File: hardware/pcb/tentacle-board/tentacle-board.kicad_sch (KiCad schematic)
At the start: 32 parts, among them J1 USB_B_Micro, J2 Conn_01x02, U1 NCP1117-3.3_SOT223, U2 W25Q128JVS, U3 RP2040, Y1 ABLS-12.000MHZ-B4-T

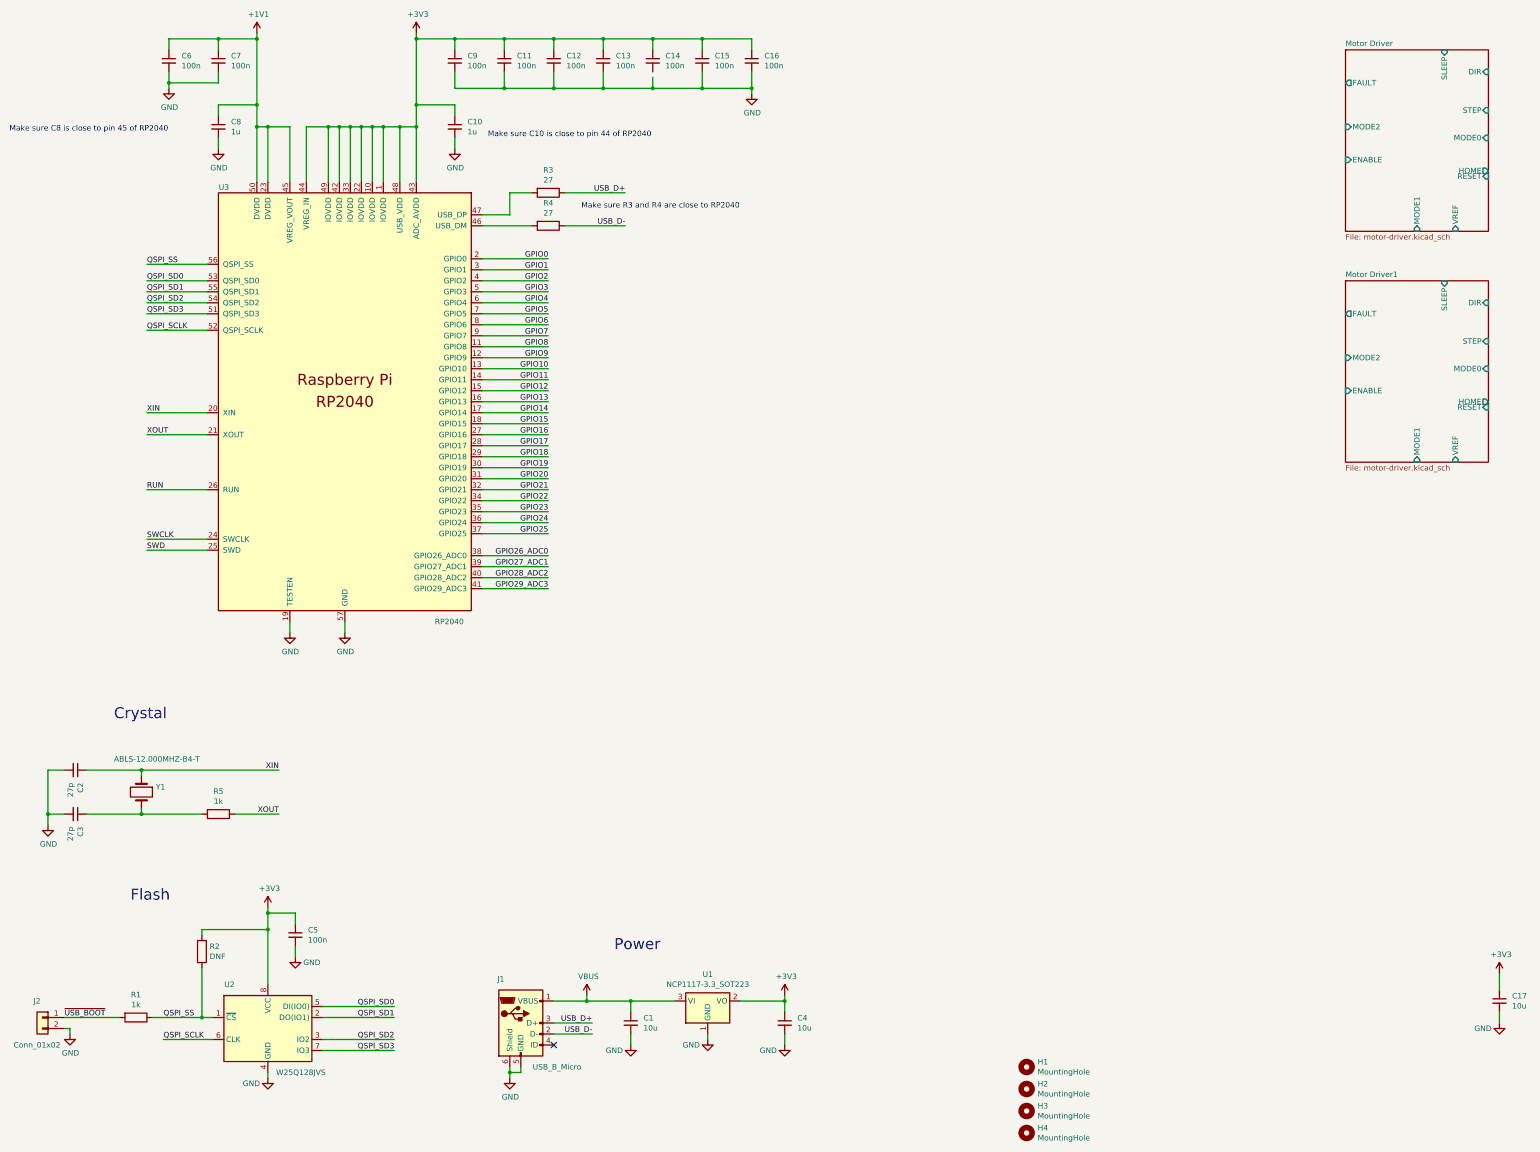
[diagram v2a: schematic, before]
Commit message: Added the MCU and supporting components and wired them up
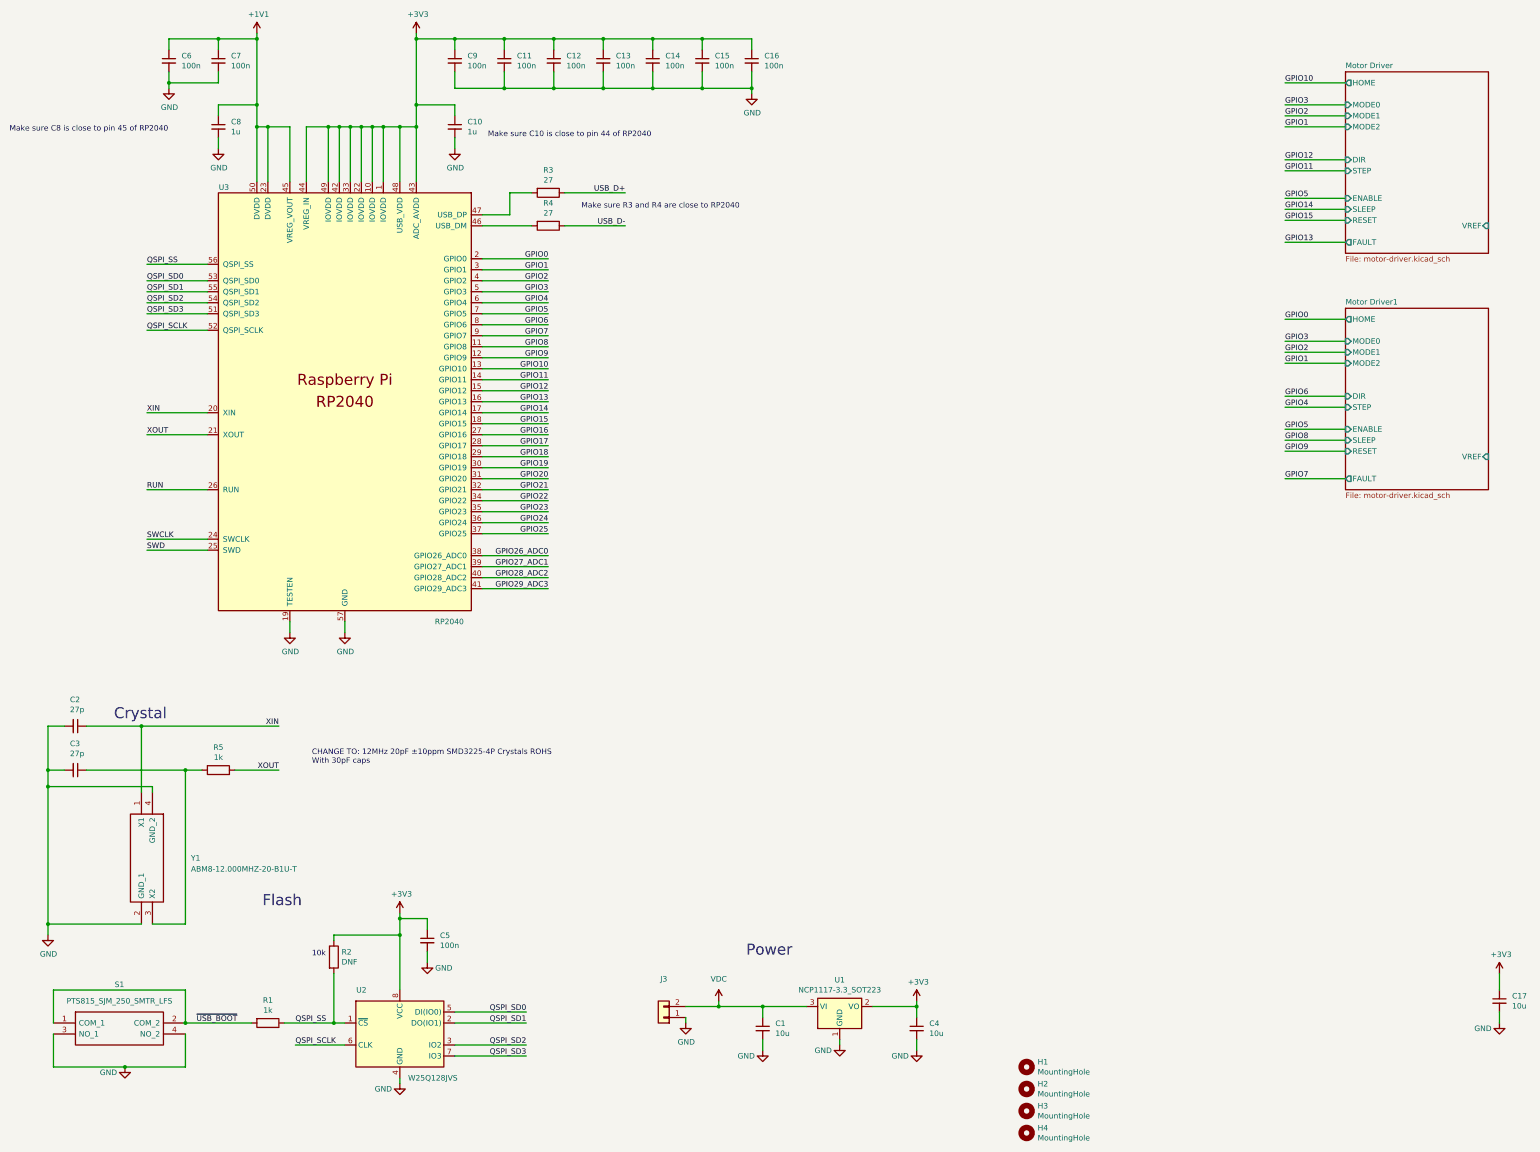
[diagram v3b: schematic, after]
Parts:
- removed J1: USB_B_Micro, RP2040_minimal:USB_Micro-B_Amphenol_10103594-0001LF_Horizontal_modified, symbol tentacle-board-rescue:USB_B_Micro-Connector
- removed J2: Conn_01x02, Connector_PinHeader_2.54mm:PinHeader_1x02_P2.54mm_Vertical, symbol Connector_Generic:Conn_01x02
- removed Y1: ABLS-12.000MHZ-B4-T, RP2040_minimal:Crystal_SMD_HC49-US, symbol Device:Crystal
- added J3: Conn_01x02, Connector_JST:JST_XH_B2B-XH-A_1x02_P2.50mm_Vertical, symbol Connector_Generic:Conn_01x02
- added S1: PTS815_SJM_250_SMTR_LFS, tentacle-board:PTS815SJM250SMTRLFS, symbol PTS815_SJM_250_SMTR_LFS:PTS815_SJM_250_SMTR_LFS
- added Y1: ABM8-12.000MHZ-20-B1U-T, ABM810000MHZ12D2W, symbol ABM8-12.000MHZ-20-B1U-T:ABM8-12.000MHZ-20-B1U-T
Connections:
- net GND: now also C14.2, J3.1 (Pin_1), S1.3 (NO_1), S1.4 (NO_2), Y1.2 (GND_1), Y1.4 (GND_2)
- net XIN: now also Y1.1 (X1)
- net ~{USB_BOOT}: now also S1.1 (COM_1), S1.2 (COM_2)
- net at C3.1, R5.2: now also Y1.3 (X2)
- net VBUS renamed VDC
- net VDC: now also J3.2 (Pin_2)
- no-connect marks 1 -> 0
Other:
- note added: "10k"
- note added: "CHANGE TO: 12MHz 20pF ±10ppm SMD3225-4P Crystals ROHS With 30pF caps"
- moved on the sheet: C1, C2, C3, C4, C5, R1, R2, R5, U1, U2

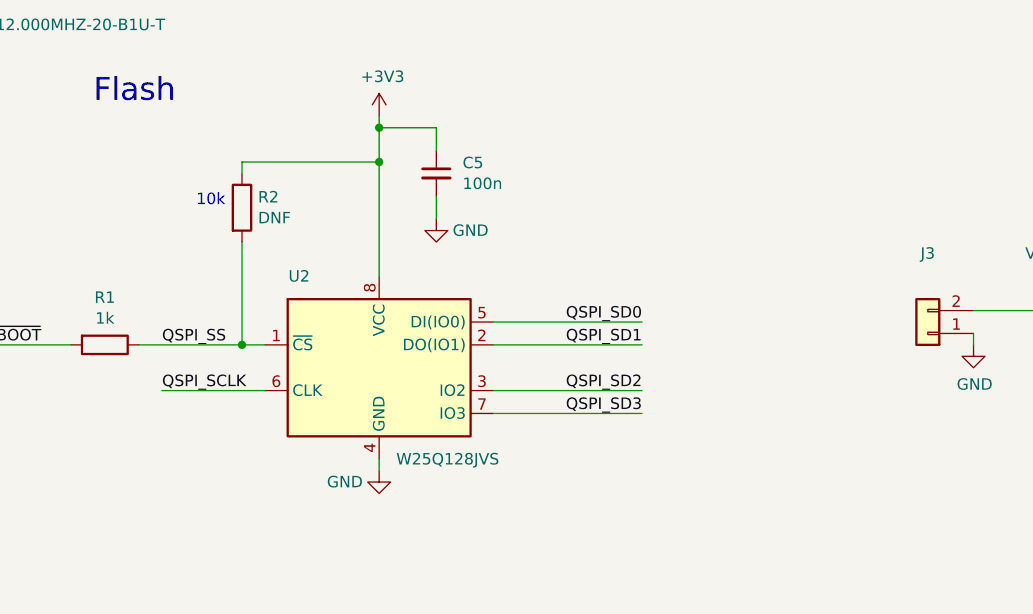
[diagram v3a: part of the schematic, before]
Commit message: Updated flash to a smaller package, moved in the MCU to make some more room
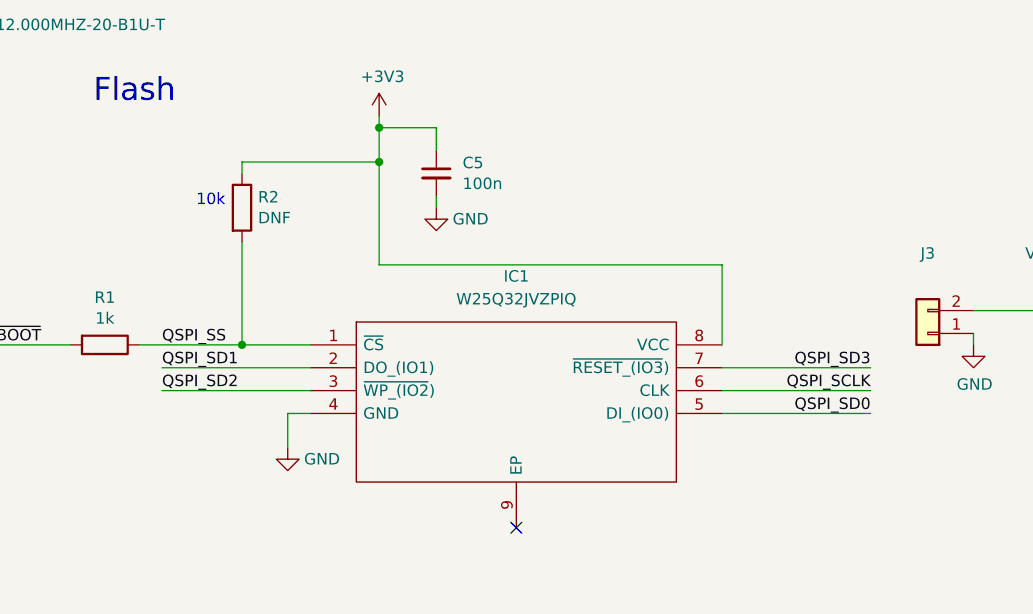
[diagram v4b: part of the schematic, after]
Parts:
- removed U2: W25Q128JVS, Package_SO:SOIC-8_5.23x5.23mm_P1.27mm, symbol tentacle-board-rescue:W25Q128JVS-Memory_Flash
- added IC1: W25Q32JVZPIQ, SON127P600X500X80-9N-D, symbol W25Q32JVZPIQ:W25Q32JVZPIQ
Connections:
- net +3V3: now also IC1.8 (VCC)
- net GND: now also IC1.4 (GND)
- net QSPI_SCLK: now also IC1.6 (CLK)
- net QSPI_SD0: now also IC1.5 (DI_(IO0))
- net QSPI_SD1: now also IC1.2 (DO_(IO1))
- net QSPI_SD2: now also IC1.3 (~{WP_(IO2}))
- net QSPI_SD3: now also IC1.7 (~{RESET_(IO3}))
- net QSPI_SS: now also IC1.1 (~{CS})
- no-connect marks 0 -> 1

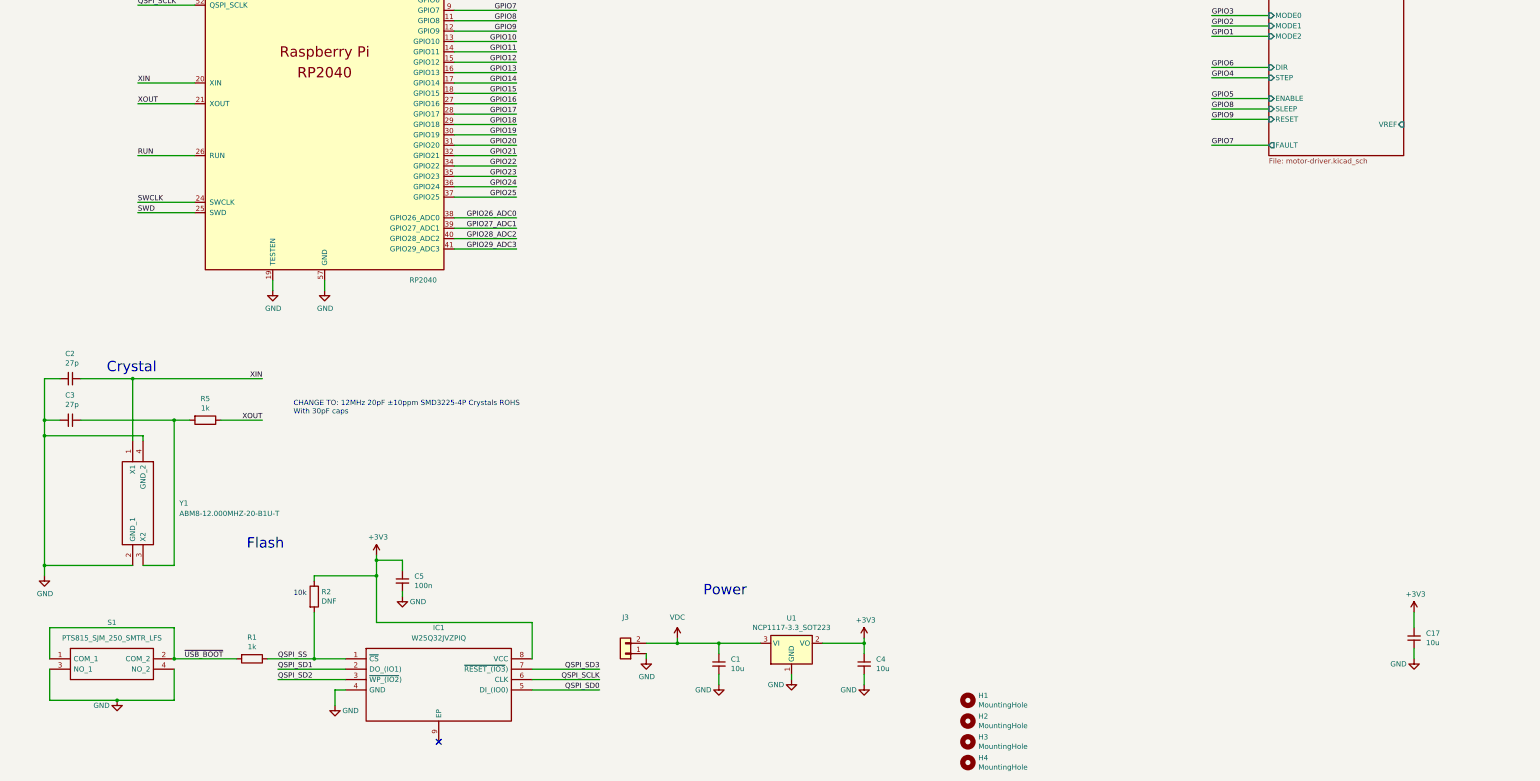
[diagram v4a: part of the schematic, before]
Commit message: Added aux plugs and updated the edge cuts
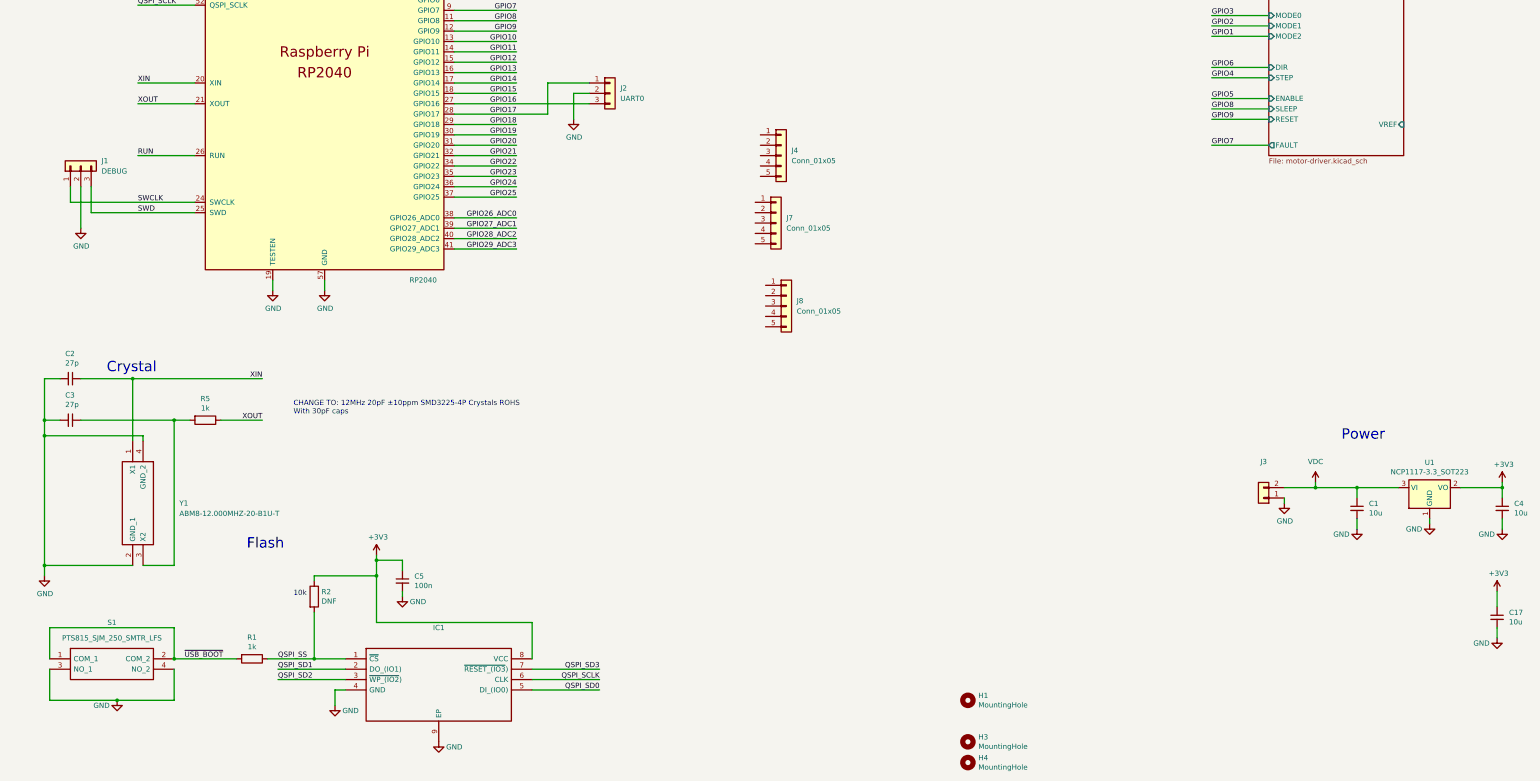
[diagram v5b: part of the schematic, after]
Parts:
- removed H2: MountingHole, MountingHole:MountingHole_2.7mm_M2.5, symbol Mechanical:MountingHole
- added J1: DEBUG, Connector_JST:JST_SH_BM03B-SRSS-TB_1x03-1MP_P1.00mm_Vertical, symbol Connector_Generic:Conn_01x03
- added J2: UART0, Connector_JST:JST_SH_BM03B-SRSS-TB_1x03-1MP_P1.00mm_Vertical, symbol Connector_Generic:Conn_01x03
- added J4, J7, J8: Conn_01x05, Connector_JST:JST_SH_BM05B-SRSS-TB_1x05-1MP_P1.00mm_Vertical, symbol Connector_Generic:Conn_01x05
- H1, H3, H4: footprint MountingHole:MountingHole_2.7mm_M2.5 -> MountingHole:MountingHole_2.2mm_M2_ISO7380_Pad_TopBottom
- IC1: LCSC # (none) -> C571260; Manufacturer_Part_Number W25Q32JVZPIQ -> (none); Mfr # (none) -> W25Q32JVZPIQ; Mouser # (none) -> 454-W25Q32JVZPIQ; Mouser Part Number 454-W25Q32JVZPIQ -> (none)
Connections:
- net GND: now also IC1.9 (EP), J1.2 (Pin_2), J2.2 (Pin_2)
- net GPIO16: now also J2.3 (Pin_3)
- net GPIO17: now also J2.1 (Pin_1)
- net SWCLK: now also J1.1 (Pin_1)
- net SWD: now also J1.3 (Pin_3)
- no-connect marks 1 -> 0
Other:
- moved on the sheet: C1, C17, C4, J3, U1
